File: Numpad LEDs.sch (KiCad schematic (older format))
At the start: 42 parts

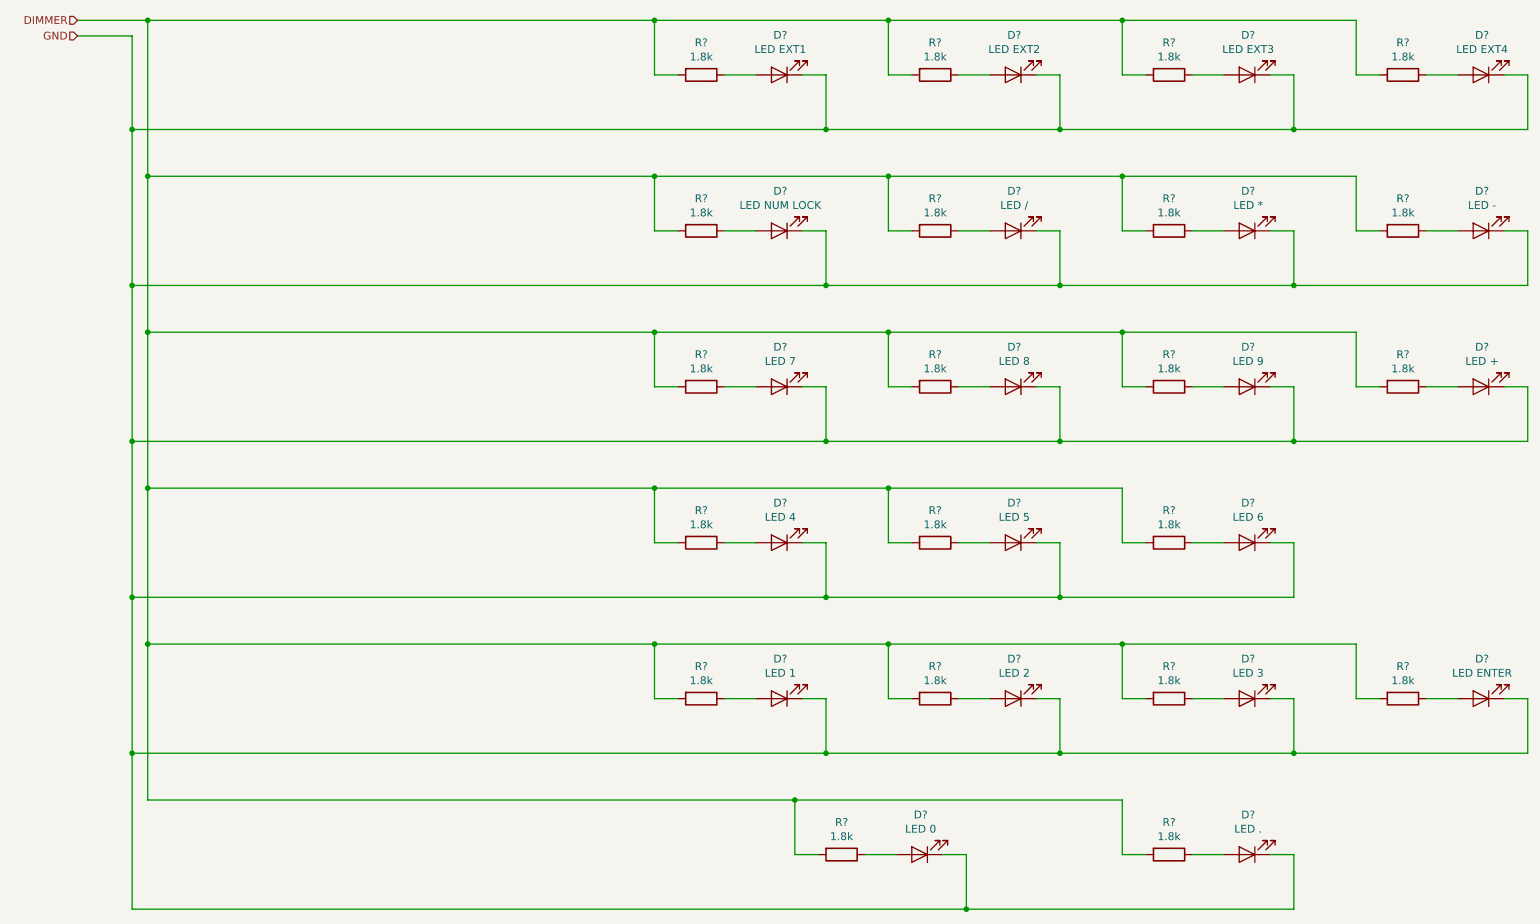
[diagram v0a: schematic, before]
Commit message: Corrected errors found in design rule check
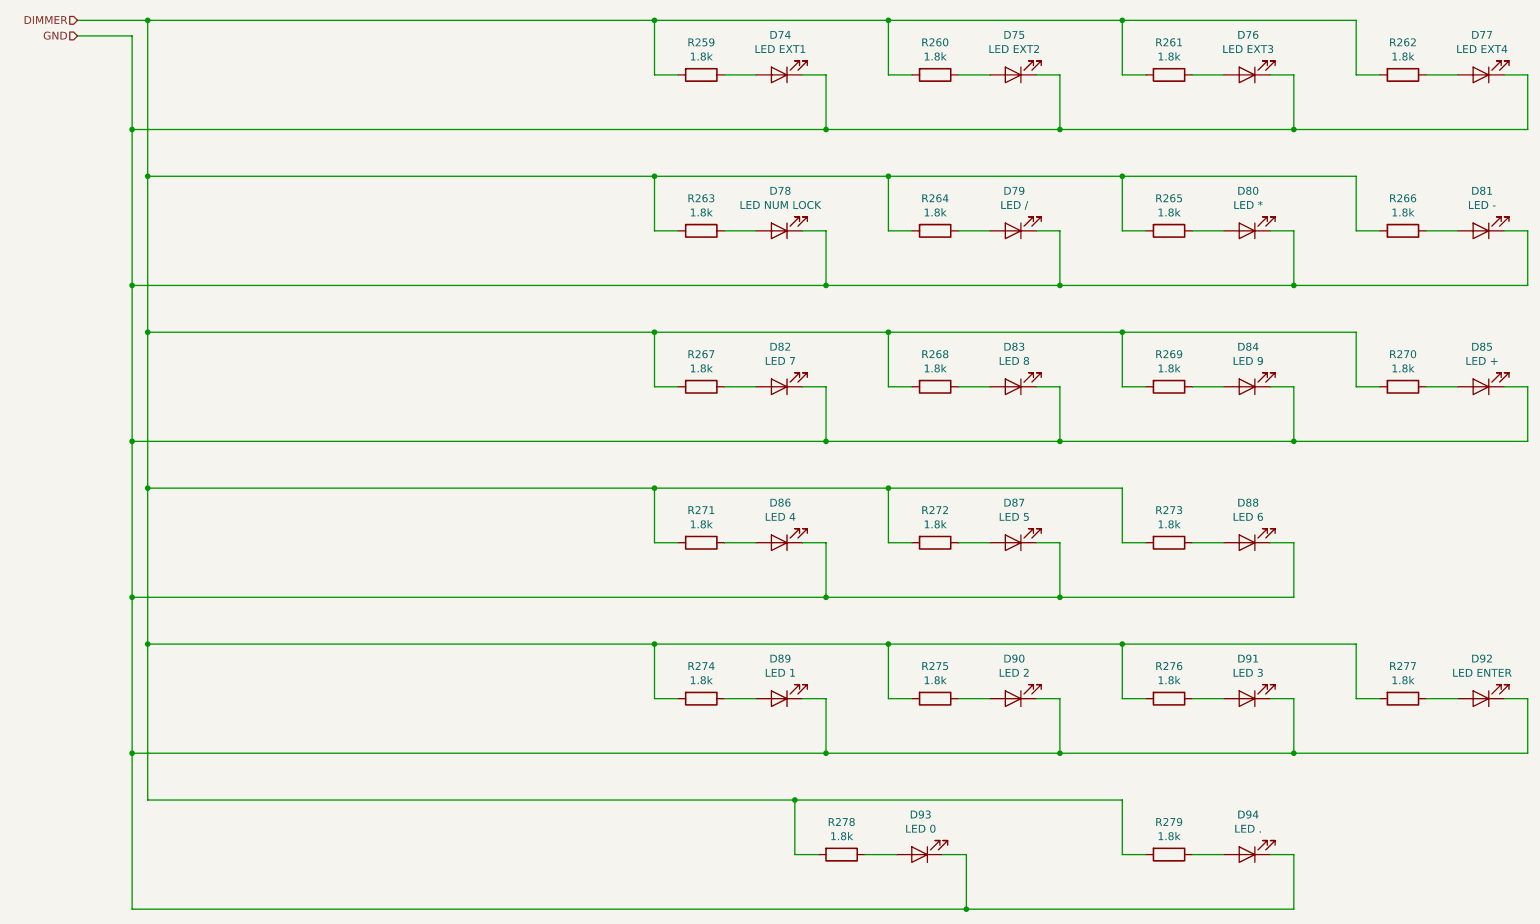
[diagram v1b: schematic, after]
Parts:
- D74, D75, D76, D77, D78, D79, D80, D81, D82, D83, D84, D85, D86, D87, D88, D89, D90, D91, D92, D93, D94: renamed from D?; footprint (none) -> LED_SMD:LED_1206_3216Metric_ReverseMount_Hole1.8x2.4mm
- R259, R260, R261, R262, R263, R264, R265, R266, R267, R268, R269, R270, R271, R272, R273, R274, R275, R276, R277, R278, R279: renamed from R?; footprint (none) -> Resistor_SMD:R_1206_3216Metric_Pad1.42x1.75mm_HandSolder

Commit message: Redesigned for single large PCB
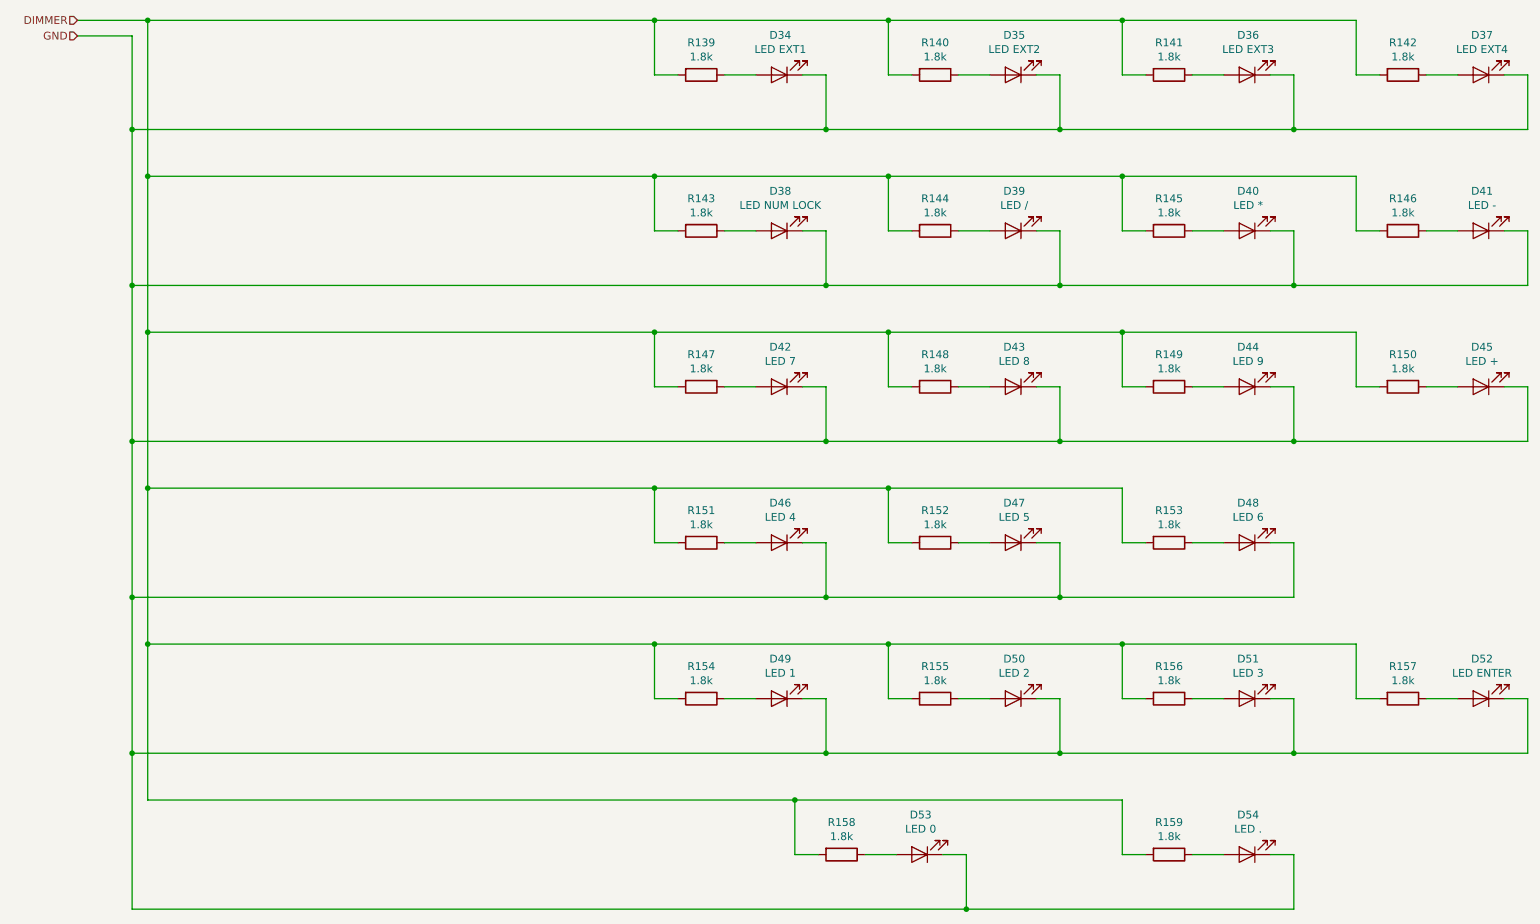
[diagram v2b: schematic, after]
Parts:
- renumbered D74 to D34, D75 to D35, D76 to D36, D77 to D37, D78 to D38, D79 to D39, D80 to D40, D81 to D41, D82 to D42, D83 to D43, D84 to D44, D85 to D45, D86 to D46, D87 to D47, D88 to D48, D89 to D49, D90 to D50, D91 to D51, D92 to D52, D93 to D53, D94 to D54, R259 to R139, R260 to R140, R261 to R141, R262 to R142, R263 to R143, R264 to R144, R265 to R145, R266 to R146, R267 to R147, R268 to R148, R269 to R149, R270 to R150, R271 to R151, R272 to R152, R273 to R153, R274 to R154, R275 to R155, R276 to R156, R277 to R157, R278 to R158, R279 to R159
